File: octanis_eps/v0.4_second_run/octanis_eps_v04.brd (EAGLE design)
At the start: 63.7 x 49.6 mm, 107 parts, among them IC1 OPA2333DGK, IC5 OPA2333DGK, IC7 OPA2333DGK, IC9 OPA2333DGK, Q1 FC-12M, Q2 N-HEXFET-2D_SOT232-, Q3 N-HEXFET-2D_SOT232-, Q4 N-HEXFET-2D_SOT232-

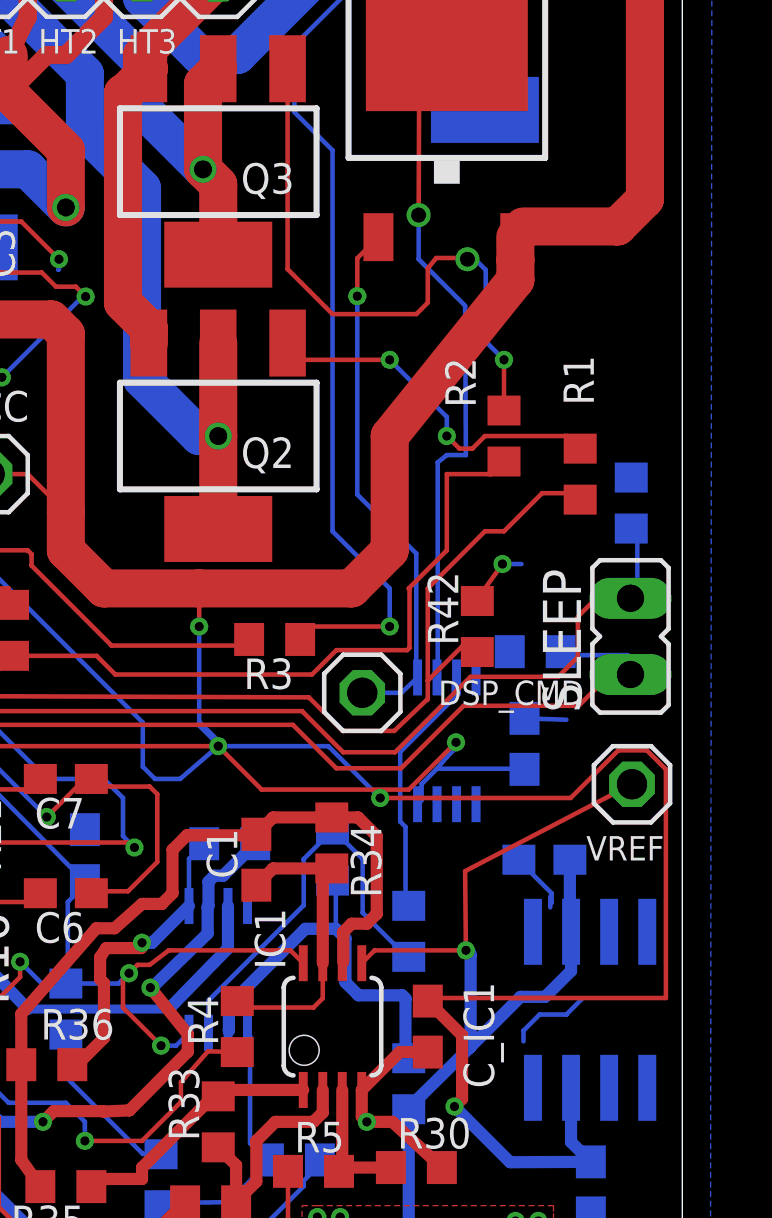
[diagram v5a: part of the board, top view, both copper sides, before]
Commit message: changed IC9A=OPA2333 (2ch) for IC9=0PA347 with SC70-5 small outline package. OPA347 allows for bigger driving currents so to be able to drive the POWER N-FET on disispation CMD (cf bgeissma for details), modifications still to be performed on the boost converter circuit
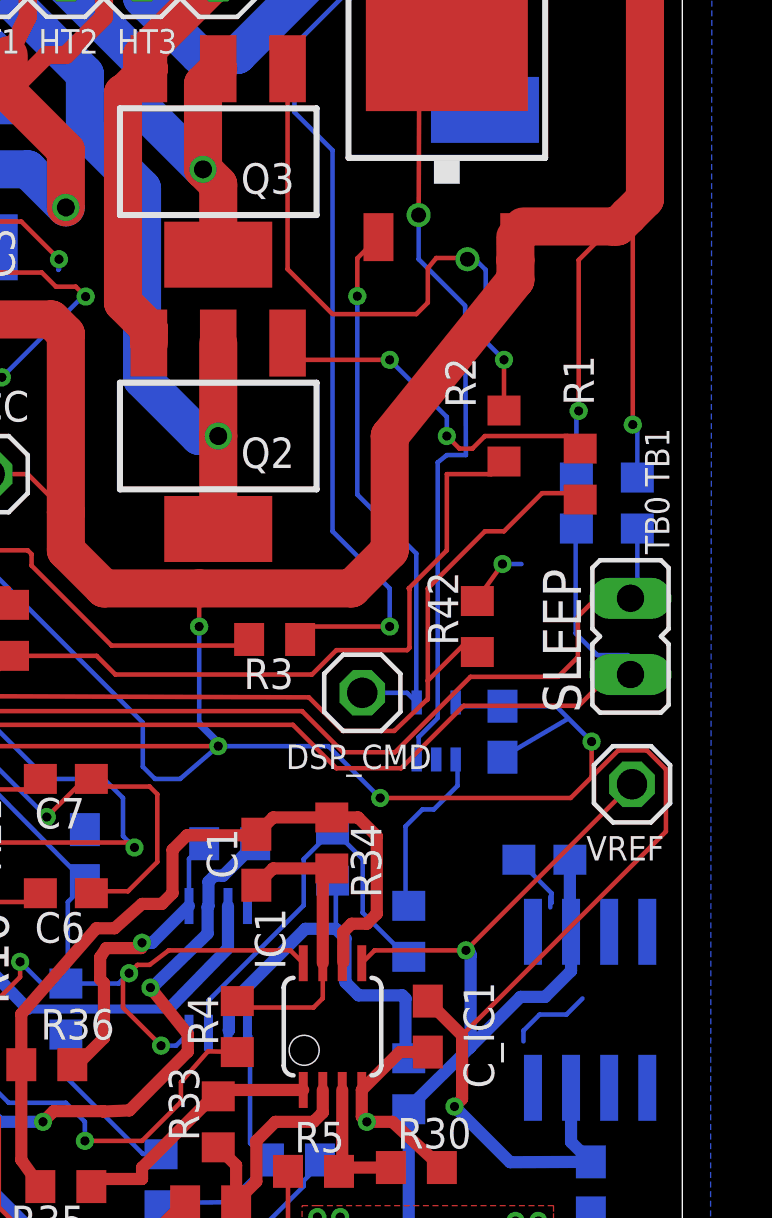
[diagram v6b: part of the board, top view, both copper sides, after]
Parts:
- IC9: value OPA2333DGK -> OPA347; device linear:MSOP08 -> Octanis1_EPS:SC70-5
- moved R8 5.14 mm to (60.2, 56.2), turned to 90 degrees
- moved C_IC9 0.84 mm to (57.7, 48.6), turned to 90 degrees
- moved IC9 0.49 mm to (55.5, 48.6), turned to 0 degrees
- moved R37 0.20 mm to (62.2, 56.2)
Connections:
- net N$27 renamed TB1
- net N$36 renamed TB0
- net DISSIP: now also IC9.3; no longer IC9.2
- net GND: now also IC9.2; no longer IC9.4, R37.2, R8.2
- net N$22: now also IC9.1; no longer IC9.3
- net N$45: now also IC9.4; no longer IC9.1
- net VCC: now also IC9.6, R37.2, R8.2; no longer IC9.8
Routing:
- net VCC: track 385.3 -> 390.5 mm, vias 16 -> 18
- net TB1: track 41.4 -> 44.6 mm
- net DISSIP: track 35.3 -> 38.3 mm
- net N$22: track 8.49 -> 5.88 mm
- net VREF: track 61.6 -> 60.5 mm
- net GND: track 239.7 -> 240.8 mm
- net N$45: track 17.9 -> 18.6 mm
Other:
- board text added: "TB0 TB1"

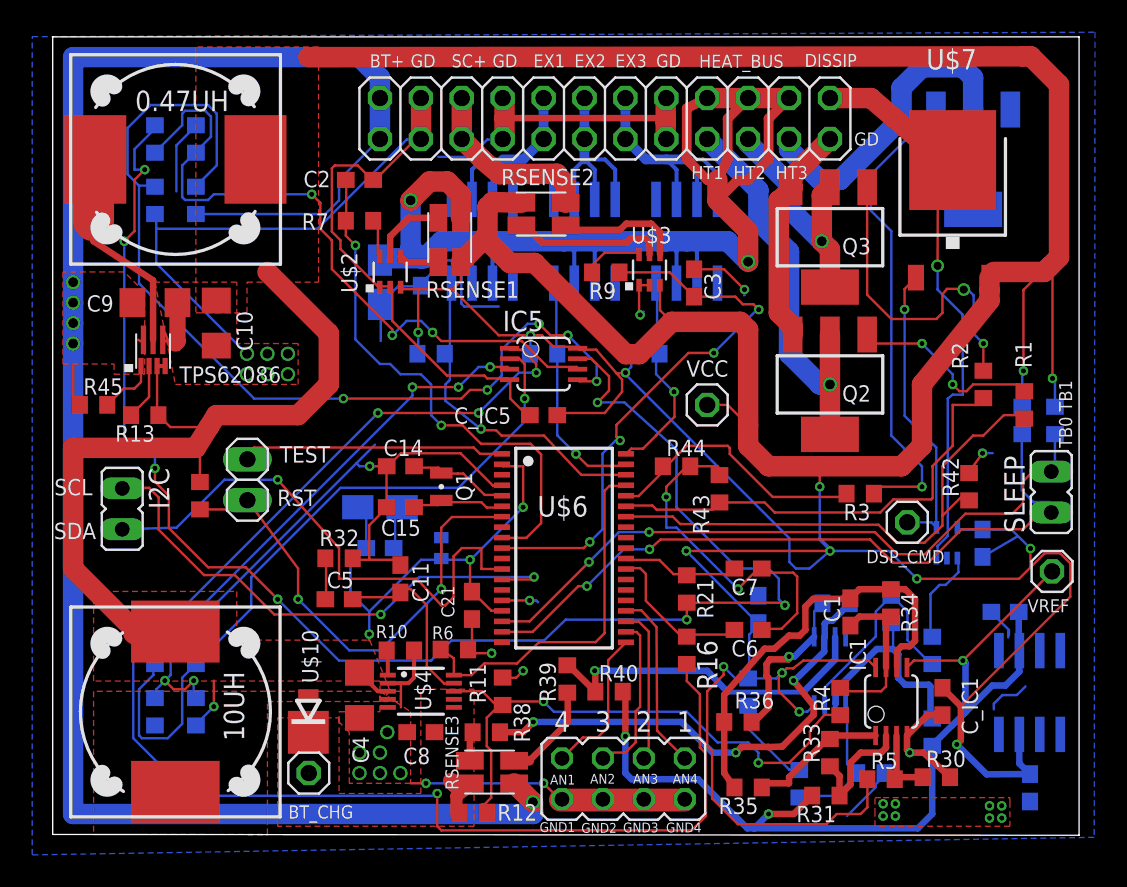
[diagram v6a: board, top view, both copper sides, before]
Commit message: re-routed EPS. adapted silkscreen on EPS
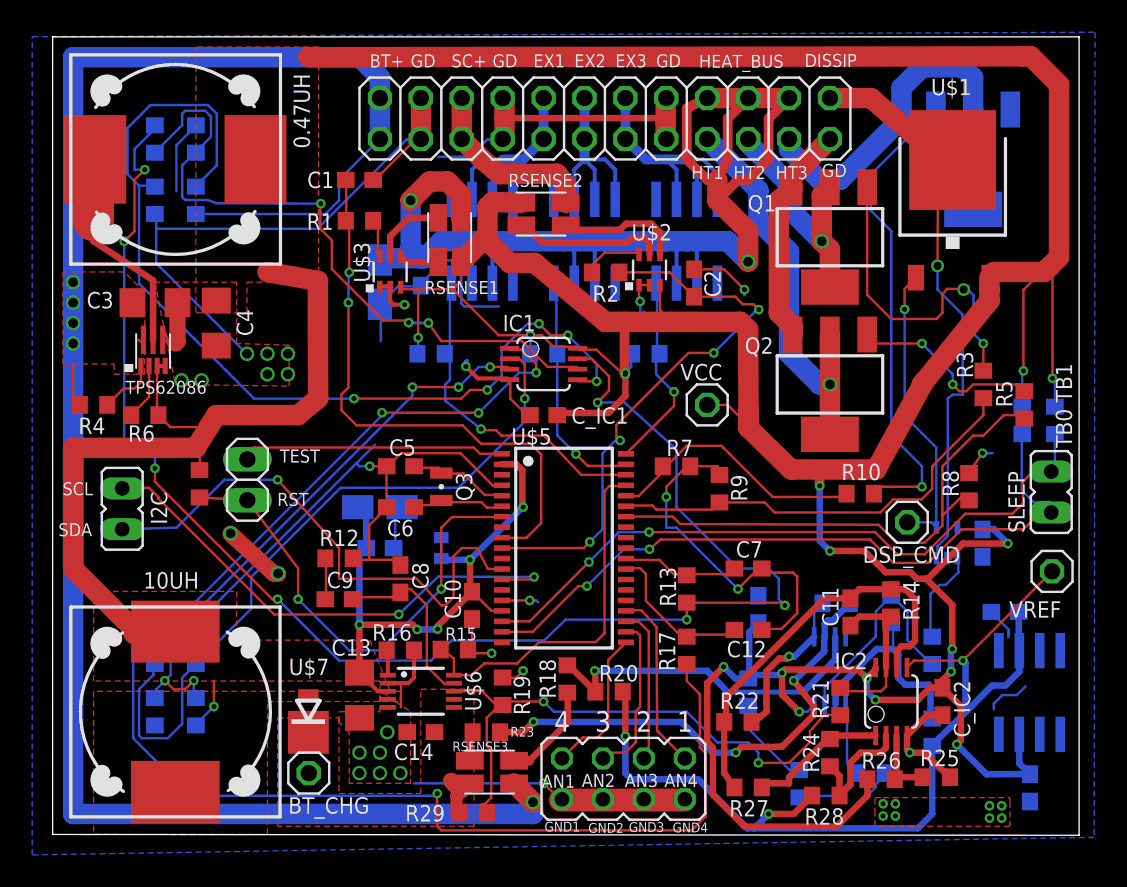
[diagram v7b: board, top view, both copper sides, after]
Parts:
- removed C15: 12pF, rcl:C0603
- removed C21, C_IC5: 100nF, rcl:C0603
- removed IC5: OPA2333DGK, linear:MSOP08
- removed JP7: d SBW clk, pinhead:1X02
- removed R30: 20k, rcl:R0603
- removed R31: 23.2k, rcl:R0603
- removed R32: 82k, rcl:R0603
- removed R33, R42, R43, R44: 1M, rcl:R0603
- removed R34, R35, R36: 162k, rcl:R0603
- removed R38, R39, R46: 10k, rcl:R0603
- removed R40: 920k, rcl:R0603
- removed R45: 0Ohm, rcl:R0603
- removed RSENSE3: RSENSE3, Octanis1_EPS:4PADS_RESISTOR
- removed U$10: MBRM120LTIG, Octanis1_EPS:DO216AA
- added C12: 1.5uF, rcl:C0603
- added C13: 4.7u, rcl:C1206
- added C_IC2: 100nF, rcl:C0603
- added IC2: OPA2333DGK, linear:MSOP08
- added JP3: (no value), jumper:JP4Q
- added R100: 953, rcl:R0603
- added R101: 86k6, rcl:R0603
- added R102: 4k02, rcl:R0603
- added R103, R107, R116, R118: 200k, rcl:R0603
- added R104, R108, R112, R117, R119: 100k, rcl:R0603
- added R105: 147k, rcl:R0603
- added R106: 3k32, rcl:R0603
- added R109: 560k, rcl:R0603
- added RSENSE1: RSENSE2, Octanis1_EPS:4PADS_RESISTOR
- added U$100: MAX6190BESA, Octanis1_EPS:SO8
- C1: value 10nF -> 1.5uF
- C10: value 22u -> 100nF; device rcl:C1206 -> rcl:C0603
- C11: value 4.7p -> 10nF
- C14: value 12pF -> 22u
- C3: value 1.5uF -> 10u; device rcl:C0603 -> rcl:C1206
- C4: value 4.7u -> 22u
- C5: value 470p -> 12pF
- C6: value 1.5uF -> 12pF
- C8: value 22u -> 4.7p
- C9: value 10u -> 470p; device rcl:C1206 -> rcl:C0603
- JP2: value (none) -> d SBW clk; device jumper:JP4Q -> pinhead:1X02
- Q1: value FC-12M -> N-HEXFET-2D_SOT232-; device crystal:FC-12M -> transistor-power:SOT223
- Q3: value N-HEXFET-2D_SOT232- -> FC-12M; device transistor-power:SOT223 -> crystal:FC-12M
- R10: value 30.1k -> 1k
- R11, R18, R23: value 100k -> 10k
- R12: value 200k -> 82k
- R13: value 1M -> 1k
- R14, R22: value 200k -> 162k
- R16: value 1k -> 30.1k
- R17: value 200k -> 1k
- R19: value 200k -> 100k
- R20: value 100k -> 920k
- R21: value 1k -> 560k
- R24: value 147k -> 1M
- R25: value 953 -> 20k
- R26: value 86k6 -> 31.60k
- R27: value 4k02 -> 162k
- R28: value 560k -> 23.2k
- R29: value 3k32 -> 200k
- R4: value 560k -> 0Ohm
- R5: value 31.60k -> 1k
- R6, R8: value 100k -> 1M
- R7, R9: value 1k -> 1M
- RSENSE2: value RSENSE2 -> RSENSE3
- U$1: value MAX6190BESA -> MJD44H11T0-252; device Octanis1_EPS:SO8 -> Octanis1_EPS:TO252
- U$4: value LTC3402 -> TPS62086; device Octanis1_EPS:MSOP10 -> Octanis1_EPS:QFN-7
- U$5: value TPS62086 -> MSP430G2544; device Octanis1_EPS:QFN-7 -> Octanis1_EPS:TSSOP38_MSPGXX44_SERIES
- U$6: value MSP430G2544 -> LTC3402; device Octanis1_EPS:TSSOP38_MSPGXX44_SERIES -> Octanis1_EPS:MSOP10
- U$7: value MJD44H11T0-252 -> MBRM120LTIG; device Octanis1_EPS:TO252 -> Octanis1_EPS:DO216AA
- moved U$7 51.9 mm to (15.9, 36.8), turned to 90 degrees
- moved R4 49.9 mm to (2.54, 57.1), turned to 0 degrees
- moved R22 49.4 mm to (42.5, 37.5), flipped to the top, turned to 180 degrees
- moved R14 43.7 mm to (52.0, 44.9), flipped to the top
- moved R1 42.8 mm to (19.1, 68.6), turned to 0 degrees
- moved R23 42.2 mm to (26.9, 36.8), flipped to the top, turned to 0 degrees
- moved R20 41.5 mm to (34.5, 39.3), flipped to the top, turned to 0 degrees
- moved C1 40.6 mm to (19.1, 71.1), turned to 180 degrees
- moved R19 35.9 mm to (27.9, 39.4), flipped to the top
- moved R13 35.3 mm to (39.4, 45.7), turned to 270 degrees
- moved RSENSE2 34.8 mm to (28.7, 35.1)
- moved C3 33.5 mm to (6.35, 63.5), turned to 180 degrees
- moved U$1 30.9 mm to (55.9, 69.8), flipped to the top
- moved C_IC1 30.5 mm to (30.5, 56.5), turned to 0 degrees
- moved R17 30.5 mm to (39.4, 41.9), flipped to the top, turned to 270 degrees
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- renumbered C22 to C102, C24 to C103, C26 to C104, C27 to C100, C28 to C101, C29 to C105, C_IC7 to C_IC100, C_IC9 to C_IC101, IC7 to IC100, IC9 to IC101, Q4 to Q100, R37 to R111, R41 to R110, R79 to R113, R80 to R114, R81 to R115, U$16 to U$103, U$17 to U$102, U$18 to U$101
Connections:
- net A_EXT1: now also JP3.7, U$5.20; no longer JP2.7, U$6.20
- net A_EXT2: now also JP3.5, U$5.21; no longer JP2.5, U$6.21
- net A_EXT3: now also JP3.3, U$5.22; no longer JP2.3, U$6.22
- net A_EXT4: now also JP3.1, U$5.23; no longer JP2.1, U$6.23
- net BT+: now also C3.2, R116.2, R4.1, RSENSE2.V1, U$4.7; no longer C9.2, R19.2, R45.1, RSENSE3.V1, U$5.7
- net BT_CHG: now also C14.2, R29.1, RSENSE2.V2, U$6.7, U$7.C; no longer C8.2, R12.1, RSENSE3.V2, U$10.C, U$4.7
- net CHG_CMD: now also C11.1, IC2.7, R14.2, R21.2; no longer C1.1, IC1.7, R34.2, R4.2
- net DISSIP: now also U$1.3; no longer U$7.3
- net EN_CHG: now also R15.1, U$5.35, U$6.10; no longer R6.1, U$4.10, U$6.35
- net EN_EXT1: now also U$5.36; no longer U$6.36
- net EN_EXT2: now also U$5.37; no longer U$6.37
- net EN_EXT3: now also U$5.38; no longer U$6.38
- net EN_HEAT1: now also R5.2, R8.1, U$5.32; no longer R1.2, R42.1, U$6.32
- net EN_HEAT2: now also R3.2, R9.1, U$5.33; no longer R2.2, R43.1, U$6.33
- net EN_HEAT3: now also R10.2, R7.1, U$5.34; no longer R3.2, R44.1, U$6.34
- net GND: now also C1.1, C12.1, C13.1, C14.1, C5.2, C6.2, C_IC2.1, IC2.4, JP3.2, JP3.4, JP3.6, JP3.8, Q1.3, R101.2, R104.1, R107.2, R117.1, R118.2, R12.2, R15.2, R16.2, R19.1, R25.2, R7.2, R8.2, R9.2, U$100.4, U$5.15, U$5.4, U$6.2, U$6.5; no longer C11.1, C14.2, C15.2, C21.1, C6.1, C9.1, C_IC5.1, IC5.4, JP2.2, JP2.4, JP2.6, JP2.8, Q3.3, R10.2, R11.1, R15.1, R17.2, R20.1, R22.2, R26.2, R30.2, R32.2, R42.2, R43.2, R44.2, R6.2, U$1.4, U$4.2, U$5.5, U$6.15, U$6.4
- net HEAT2: now also Q1.2, Q1.4; no longer Q3.2, Q3.4
- net I2C_SCL: now also U$5.13; no longer U$6.13
- net I2C_SDA: now also U$5.12; no longer U$6.12
- net I_EXT_PW: now also C1.2, R1.1, U$5.9; no longer C2.2, R7.1, U$6.9
- net I_SC: now also C2.2, R2.1, U$5.10; no longer C3.2, R9.1, U$6.10
- net N$1: now also R1.2, U$3.6; no longer R7.2, U$2.6
- net N$10: now also IC1.7, R119.1, R13.2; no longer IC5.7, R21.2, R23.1
- net N$11: now also C11.2, IC2.6, R14.1, R22.2, R27.2; no longer C1.2, IC1.6, R34.1, R35.2, R36.2
- net N$12: now also IC1.1, R108.1, R17.2; no longer IC5.1, R16.2, R18.1
- net N$13: now also IC1.2, R107.1, R108.2; no longer IC5.2, R17.1, R18.2
- net N$14: now also IC1.3, R103.1, R104.2; no longer IC5.3, R14.1, R15.2
- net N$15: now also IC1.6, R118.1, R119.2; no longer IC5.6, R22.1, R23.2
- net N$16: now also IC1.5, R116.1, R117.2; no longer IC5.5, R19.1, R20.2
- net N$17: now also R23.2; no longer R38.2
- net N$18: now also R100.1, R105.2; no longer R24.2, R25.1
- net N$19: now also R100.2, R101.1; no longer R25.2, R26.1
- net N$2: now also R2.2, U$2.6; no longer R9.2, U$3.6
- net N$20: now also R102.1, R109.2; no longer R27.1, R28.2
- net N$21: now also R106.2, R109.1; no longer R28.1, R29.2
- net N$22: now also R106.1; no longer R29.1
- net N$23: now also R19.2, R21.1, R29.2, U$6.8; no longer R11.2, R12.2, R4.1, U$4.8
- net N$24: now also U$6.4, U$7.A; no longer U$10.A, U$4.4
- net N$25: now also R6.2, U$4.2; no longer R13.2, U$5.2
- net N$26: now also U$4.6; no longer U$5.6
- net N$28: now also R18.2, R20.1; no longer R39.2, R40.1
- net N$29: now also R5.1; no longer R1.1
- net N$3: now also R16.1, U$6.1; no longer R10.1, U$4.1
- net N$30: now also R4.2, U$4.1; no longer R45.2, U$5.1
- net N$31: now also Q1.1, R3.1; no longer Q3.1, R2.1
- net N$32: now also U$3.4; no longer U$2.4
- net N$33: now also U$3.5; no longer U$2.5
- net N$34: now also RSENSE1.V1, U$2.4; no longer RSENSE2.V1, U$3.4
- net N$35: now also RSENSE1.V2, U$2.5; no longer RSENSE2.V2, U$3.5
- net N$37: now also R10.1; no longer R3.1
- net N$38: now also R23.1, RSENSE2.I2; no longer R38.1, RSENSE3.I2
- net N$4: now also C9.1, R12.1; no longer C5.1, R32.1
- net N$40: now also R18.1, RSENSE2.I1; no longer R39.1, RSENSE3.I1
- net N$45: now also U$1.1; no longer U$7.1
- net N$48: now also C5.1, Q3.2, U$5.5; no longer C14.1, Q1.2, U$6.5
- net N$5: now also R22.1; no longer R36.1
- net N$50: now also C6.1, Q3.1, U$5.6; no longer C15.1, Q1.1, U$6.6
- net N$6: now also IC2.3, R25.1, R26.2; no longer IC1.3, R30.1, R5.2
- net N$7: now also IC2.2, R24.1, R28.1; no longer IC1.2, R31.1, R33.1
- net N$8: now also C8.2, C9.2, U$6.9; no longer C11.2, C5.2, U$4.9
- net N$9: now also IC2.1, R24.2, R27.1; no longer IC1.1, R33.2, R35.1
- net RST/SBWTDIO: now also JP2.1, R11.2, U$5.7; no longer JP7.1, R46.2, U$6.7
- net SC+: now also RSENSE1.I1; no longer RSENSE2.I1
- net TB0: now also U$5.17; no longer U$6.17
- net TB1: now also R112.1, U$5.18; no longer R8.1, U$6.18
- net TEST/SBWTCK: now also JP2.2, U$5.1; no longer JP7.2, U$6.1
- net VCC: now also C13.2, C_IC2.2, IC2.8, R103.2, R105.1, R11.1, R112.2, R26.1, R6.1, RSENSE1.I2, U$1.2, U$100.3, U$4.4, U$5.16, U$5.2, U$6.3; no longer C21.2, C_IC5.2, IC5.8, R13.1, R14.2, R24.1, R46.1, R5.1, R8.2, RSENSE2.I2, U$1.3, U$5.3, U$5.4, U$6.16, U$6.2, U$7.2
- net VREF: now also IC2.5, R102.2, R20.2, R28.2, U$100.6; no longer IC1.5, R27.2, R31.2, R40.2, U$1.6
- net V_BT_MS: now also R13.1, U$5.28; no longer R21.1, U$6.28
- net V_BUS_MS: now also C12.2, R17.1, U$5.27; no longer C6.2, R16.1, U$6.27
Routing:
- net VCC: track 390.5 -> 357.3 mm, vias 18 -> 23
- net GND: track 240.8 -> 225.1 mm, vias 32 -> 36
- net I_EXT_PW: track 32.8 -> 35.2 mm
- net N$10: track 96.7 -> 95.5 mm
- net I2C_SCL: track 33.1 -> 32.0 mm
- net N$15: track 43.1 -> 42.0 mm
- net N$11: track 26.7 -> 25.6 mm
- net EN_HEAT2: track 28.4 -> 27.7 mm
- net I2C_SDA: track 33.6 -> 33.1 mm
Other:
- board text removed: "TPS2022D"
